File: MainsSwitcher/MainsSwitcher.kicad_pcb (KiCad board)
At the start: 2 copper layers, 59.7 x 74.9 mm, 29 parts, among them J1 SERIAL, J2 LED_STRIP, J3 SWITCHING, J4 MAINS_IN, J5 TEMP_SEN1, J6 TEMP_SEN2, K1 Relay, P1 GPIO, Q1 MOSFET_N, Q2 MCP1700T-3302E/TT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

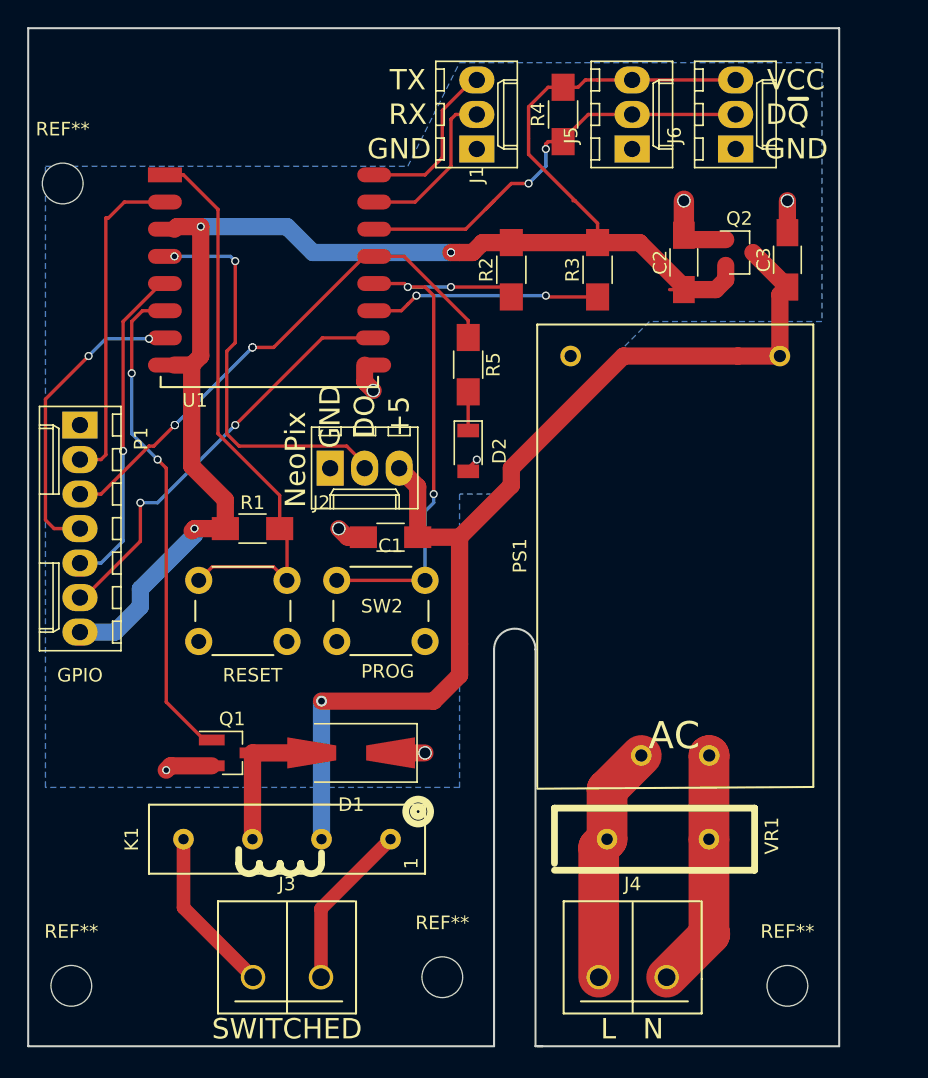
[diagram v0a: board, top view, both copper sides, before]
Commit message: Added fuseholder
Fuseholder added to the mains inlet. As ordered.
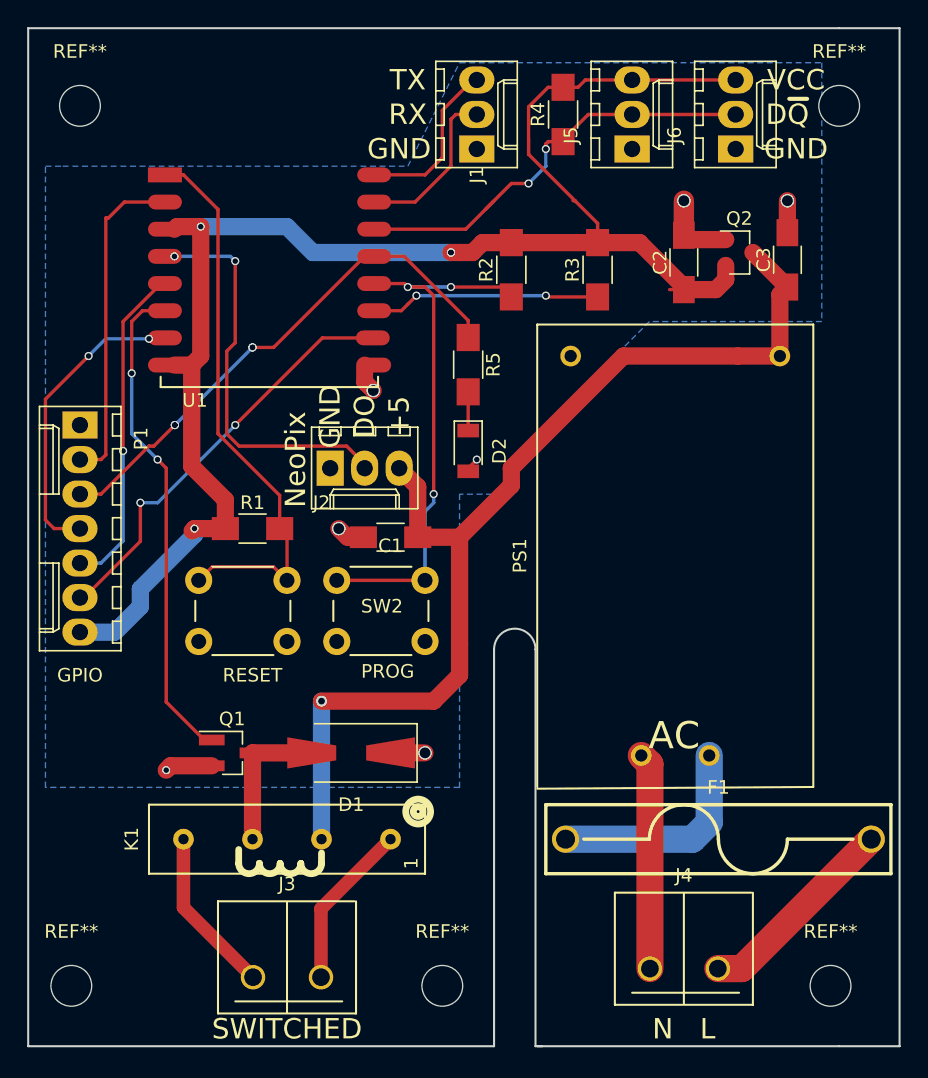
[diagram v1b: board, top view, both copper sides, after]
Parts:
- removed VR1: VR, TJS:MOV-EPCOS-B72214S0421K101
- added F1: FUSE, TJS:Schurter_Fuseholder(20x5mm)0031.8211, F.Cu at (119.4, 120.7)
- added REF**: MountingHole_3mm, Mounting_Holes:MountingHole_3mm, F.Cu at (127.6, 131.4)
- moved REF** 64.9 mm to (128.3, 66.7)
- moved REF** 5.85 mm to (72.4, 66.7)
- moved J4 3.82 mm to (116.8, 130.2)
- moved REF** 0.63 mm to (99.1, 131.4)
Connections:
- J4 pad 1: Net-(J4-Pad1) -> Net-(F1-Pad1)
- PS1 pad 2: Net-(J4-Pad1) -> Net-(F1-Pad2)
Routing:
- net Net-(J4-Pad1): track 17.7 -> 0.00 mm
- net Net-(F1-Pad2): track 0.00 -> 16.0 mm
- net Net-(F1-Pad1): track 0.00 -> 15.2 mm
- net Net-(J4-Pad2): track 17.6 -> 15.9 mm
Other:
- board size 59.7 x 74.9 mm -> 64.1 x 74.9 mm
- board text added: "DANGER LIVE MAINS"
- board text added: "N L"
- board text removed: "L N"
